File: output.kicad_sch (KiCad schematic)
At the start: 4 parts

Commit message: Cleaning up schematic
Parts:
- removed TP3: 5V Testpoint, MountingHole:MountingHole_6mm_Pad_TopBottom, symbol Connector:TestPoint
- removed TP4: 3.3v TestPoint, MountingHole:MountingHole_6mm_Pad_TopBottom, symbol Connector:TestPoint
- removed Testpoint1, Testpoint2: GND, MountingHole:MountingHole_6mm_Pad_TopBottom, symbol Connector:TestPoint
- added 3V3_HK1, 5V_HK1: TestPoint, _LVBus:HARWIN_S1751-46R, symbol Connector:TestPoint
- added C20, C21, C22: 10uf, Capacitor_SMD:C_1210_3225Metric, symbol Device:C
- added C23, C24, C27, C49, C50: 1uF, Capacitor_SMD:C_0603_1608Metric, symbol Device:C
- added C25: 10nF, Capacitor_SMD:C_0603_1608Metric, symbol Device:C
- added C26: 0.1uF, Capacitor_SMD:C_0603_1608Metric, symbol Device:C
- added C47: 4.7pF, Capacitor_SMD:C_0603_1608Metric, symbol Device:C
- added C48: 47uF, Capacitor_SMD:C_1210_3225Metric, symbol Device:C
- added D1: SMCJ26A, Diode_SMD:D_SMC, symbol Device:D_Zener
- added D2: SMF5.0A, Diode_SMD:D_SOD-123F, symbol Device:D_Zener
- added D3: SMF3.3, Diode_SMD:D_SOD-123F, symbol Device:D_Zener
- added FB5: FerriteBead, Inductor_SMD:L_1812_4532Metric, symbol Device:FerriteBead
- added L3: 1.5uH, _LVBus:Lair Inductor, symbol Device:L
- added R14: 18.22K, Resistor_SMD:R_0603_1608Metric, symbol Device:R_US
- added R15: 1M, Resistor_SMD:R_0603_1608Metric, symbol Device:R_US
- added R16: 243k, Resistor_SMD:R_0603_1608Metric, symbol Device:R_US
- added U4: LT8640SEV_PBF, _LVBus:CONV_LT8640SEV_PBF, symbol _LT8640S:LT8640SEV_PBF
- added U5: TLV75533PDBV, Package_TO_SOT_SMD:SOT-23-5, symbol Regulator_Linear:TLV75533PDBV
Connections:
- net GND: now also C20.2, C21.2, C22.2, C23.2, C24.2, C25.2, C27.2, C48.2, C49.2, C50.2, D1.2 (A), D2.2 (A), D3.2 (A), R14.2, R16.1, U4.16 (GND), U4.22 (GND), U4.25 (GND), U4.26 (GND), U4.27 (GND), U4.28 (GND), U4.3 (GND), U5.2 (GND)
- net LVBUS_3V3: now also 3V3_HK1.1, C50.1, D3.1 (K), U5.5 (OUT)
- net LVBUS_5V: now also 5V_HK1.1, C47.1, C48.1, D2.1 (K), L3.2, R15.1, U4.1 (BIAS)
- new net: C21.1, C22.1, C23.1, C24.1, FB5.2, U4.13 (VIN), U4.14 (VIN), U4.17 (EN), U4.5 (VIN), U4.6 (VIN)
- new net: C26.2, L3.1, U4.10 (SW), U4.11 (SW), U4.12 (SW), U4.8 (SW), U4.9 (SW)
- new net: R14.1, U4.18 (RT)
- new net: C27.1, U4.2 (INTVCC)
- new net: C25.1, U4.21 (TR/SS)
- new net: C47.2, R15.2, R16.2, U4.24 (FB)
- new net: C26.1, U4.7 (BST)
- new net HV_BUS: C20.1, D1.1 (K), FB5.1
- new net LV_BUS_5V: C49.1, U5.1 (IN), U5.3 (EN)
- no-connect marks 0 -> 9
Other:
- removed sheet LDO
- removed sheet buck_converter
- note added: "3V3 Regulator"
- note added: "5V Regulator"
- note added: "HV-LV Converter"
- note removed: "LVBus_3V3 Voltage"
- note removed: "LVBus_5V Voltage"

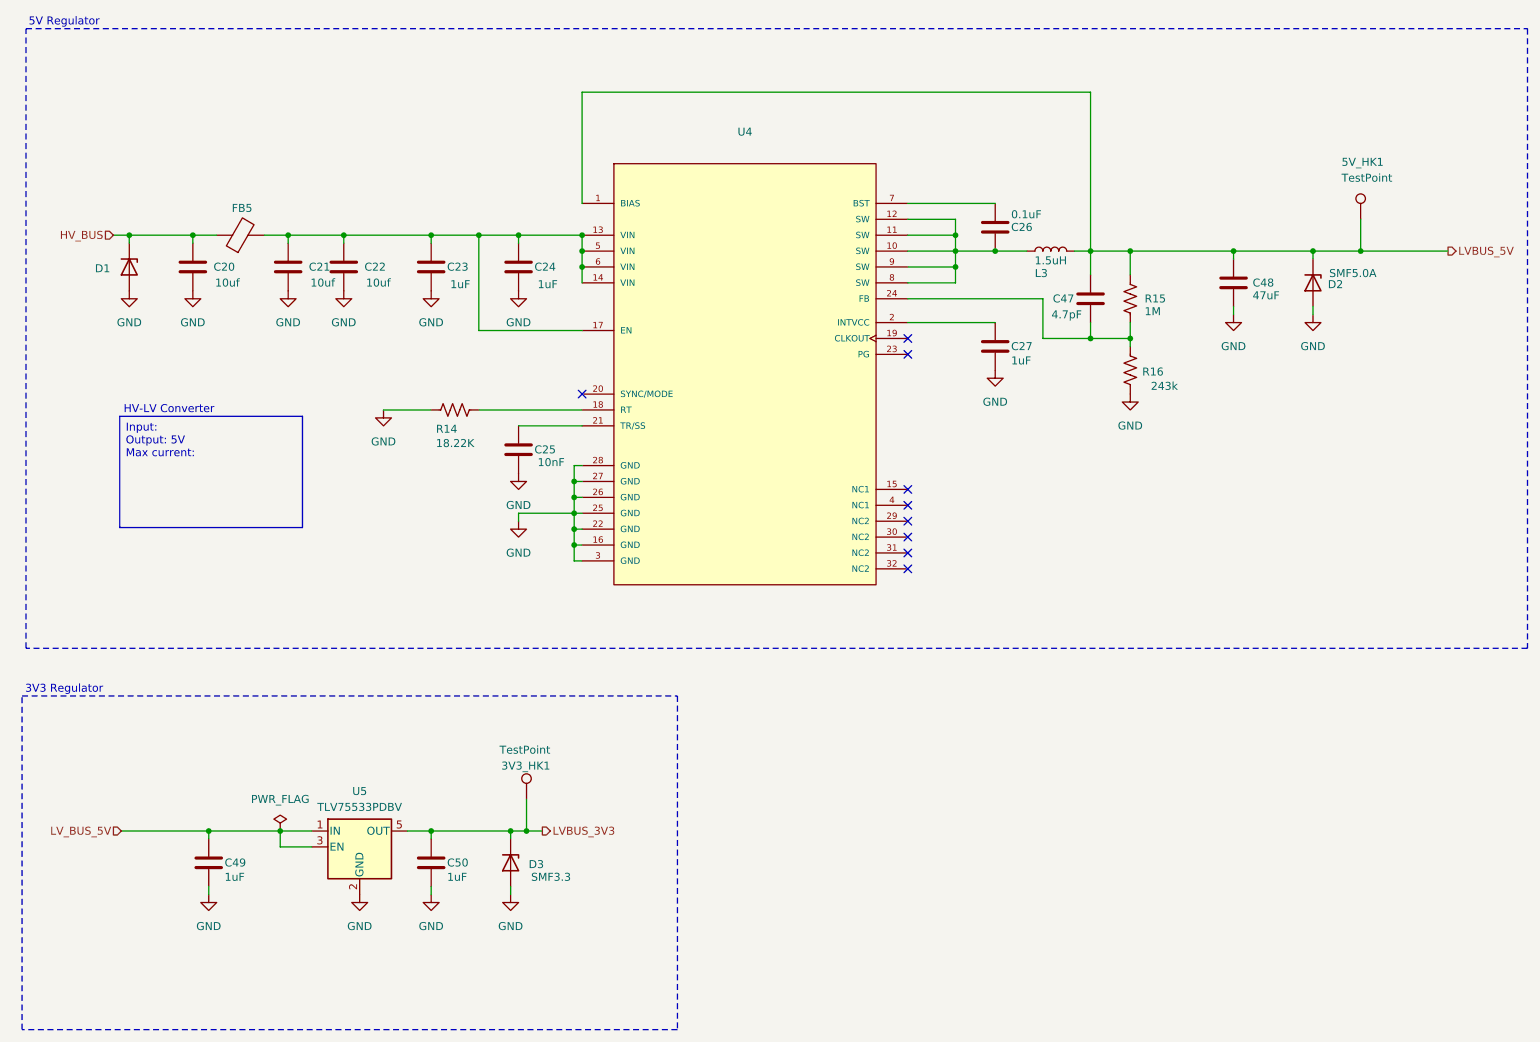
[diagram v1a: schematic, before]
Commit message: Starting bus load switch layout
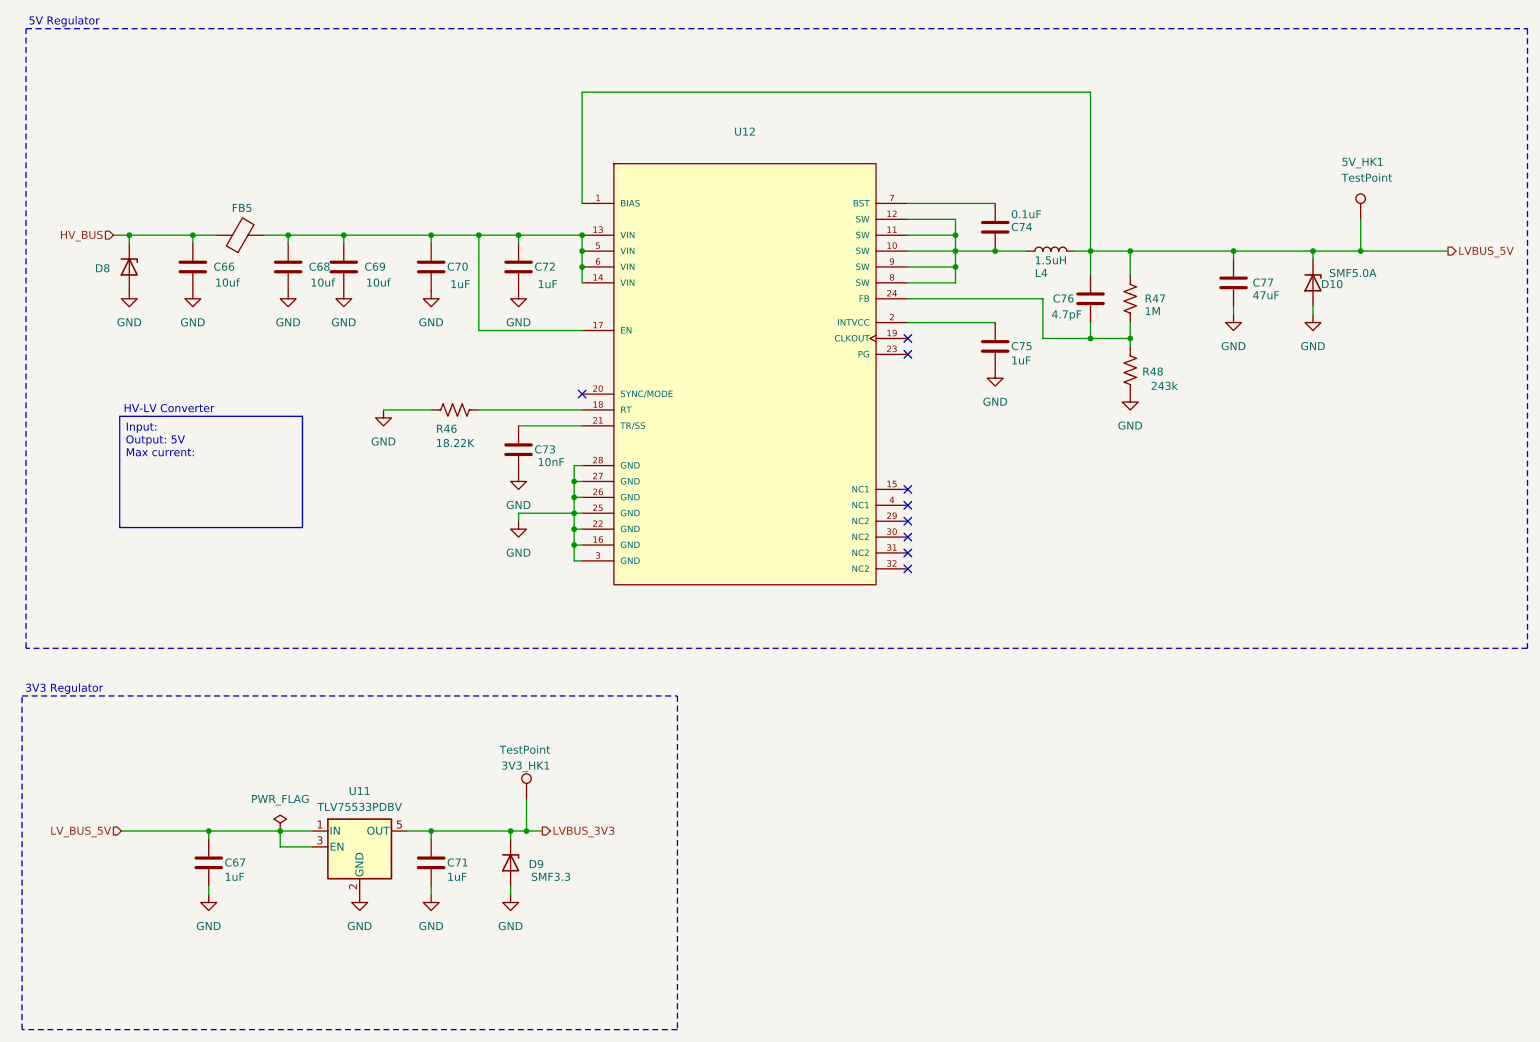
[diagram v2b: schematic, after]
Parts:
- renumbered C20 to C66, C49 to C67, C21 to C68, C22 to C69, C23 to C70, C50 to C71, C24 to C72, C25 to C73, C26 to C74, C27 to C75, C47 to C76, C48 to C77, D2 to D10, D1 to D8, D3 to D9, L3 to L4, R14 to R46, R15 to R47, R16 to R48, U5 to U11, U4 to U12

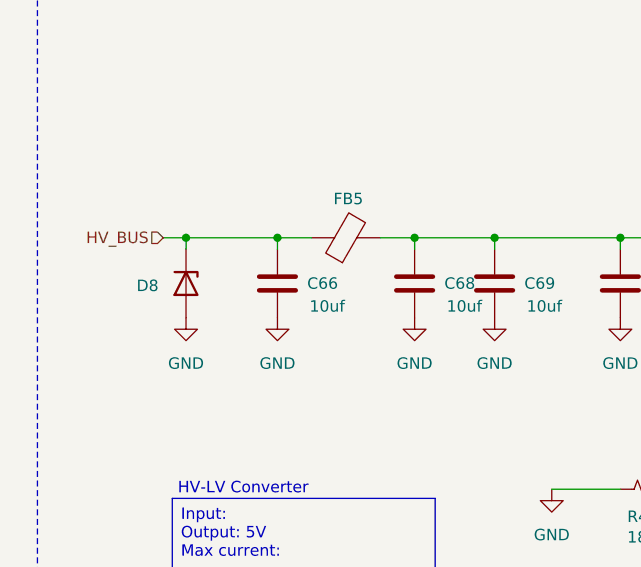
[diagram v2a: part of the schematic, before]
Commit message: Doing placement for 5V 3V3 IMU
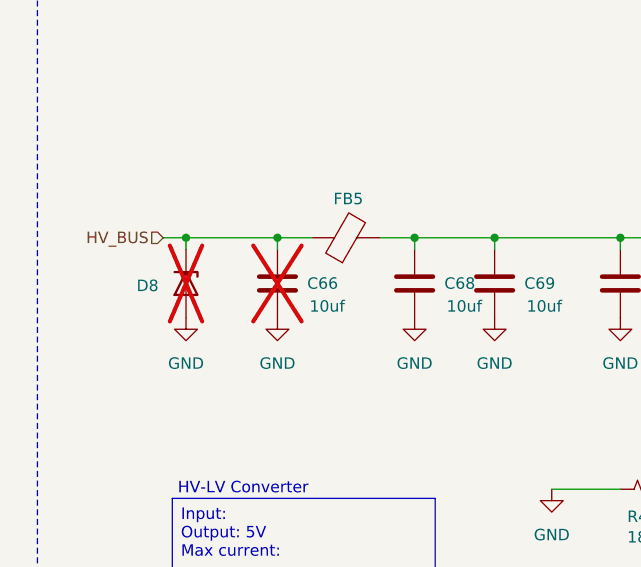
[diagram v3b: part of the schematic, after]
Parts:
- C66, D8: now not fitted; now left out of the parts list
- U12: footprint _LVBus:CONV_LT8640SEV_PBF -> _PowerBoard:CONV_LT8640SEV_PBF
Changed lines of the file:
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@@
 			)
 		)
-		(property "Footprint" "_LVBus:CONV_LT8640SEV_PBF"
+		(property "Footprint" "_PowerBoard:CONV_LT8640SEV_PBF"
 			(at 154.94 80.01 0)
 			(effects
@@
 		(unit 1)
 		(exclude_from_sim no)
-		(in_bom yes)
-		(on_board yes)
-		(dnp no)
+		(in_bom no)
+		(on_board no)
+		(dnp yes)
 		(property "Reference" "D8"
 			(at 52.832 61.214 90)
@@
 		(at 66.04 60.96 0)
 		(unit 1)
-		(exclude_from_sim no)
-		(in_bom yes)
-		(on_board yes)
-		(dnp no)
+		(exclude_from_sim yes)
+		(in_bom no)
+		(on_board no)
+		(dnp yes)
 		(property "Reference" "C66"
 			(at 69.342 60.96 0)

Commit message: Powerboard planning layout
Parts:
- removed 3V3_HK1, 5V_HK1: TestPoint, _LVBus:HARWIN_S1751-46R, symbol Connector:TestPoint
- L4: footprint _LVBus:Lair Inductor -> Inductor_SMD:Untitled

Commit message: Working on it
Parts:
- removed C74: 0.1uF, Capacitor_SMD:C_0603_1608Metric, symbol Device:C
- removed C75: 1uF, Capacitor_SMD:C_0603_1608Metric, symbol Device:C
- FB5: now not fitted; now left out of the parts list
- renumbered D8 to D10, D9 to D11, D10 to D12, R46 to R44, R47 to R45, R48 to R46
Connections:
- net LV_BUS_5V is gone; now on net +5V: C67.1, U11.1 (IN), U11.3 (EN)
- net HV_BUS: now also C68.1, C69.1, C70.1, C72.1, FB5.2, U12.13 (VIN), U12.14 (VIN), U12.17 (EN), U12.5 (VIN), U12.6 (VIN)
- net intvcc: now reaches U12.2 (INTVCC)
- net intvcc: now also U12.20 (SYNC/MODE)
- net LVBUS_3V3 renamed +3V3
- net LVBUS_5V renamed +5V
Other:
- moved on the sheet: C73, L4, R44

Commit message: Working on schematic and layout
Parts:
- renumbered C66 to C68, C67 to C69, C68 to C70, C69 to C71, C70 to C72, C71 to C73, C73 to C74, C72 to C75, R44 to R45, R45 to R46, R46 to R47, U11 to U12, U12 to U13

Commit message: Pushing
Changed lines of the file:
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@@
 		)
 	)
-	(text_box "Input:\nOutput: 5V\nMax current: "
+	(text_box "Input:\nOutput: 5V\nMax current: 6A"
 		(exclude_from_sim no)
 		(at 54.356 84.836 0)

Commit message: BOM in folder
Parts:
- C68, C70, C71: JLCPCB Status (none) -> Similar JLC in-stock package match; Mfr P/N CL32B106KBJNNWE -> CS3225X7R106K500NRL; Supplier_1 DigiKey -> LCSC; Supplier_1 P/N 1276-3388-2-ND -> C2918502; Supplier_1 Unit Price $0.22 -> (none)
- C69, C73: JLCPCB Status (none) -> JLC in-stock package match; Mfr P/N (none) -> CL10A105KB8NNNC; Supplier_1 DigiKey -> LCSC; Supplier_1 P/N 587-3247-2-ND -> C15849; Supplier_1 Unit Price $0.08 -> (none)
- C72, C75: JLCPCB Status (none) -> JLC in-stock package match; Mfr P/N UMK107AB7105KA-T -> CL10A105KB8NNNC; Supplier_1 DigiKey -> LCSC; Supplier_1 P/N 587-3247-2-ND -> C15849; Supplier_1 Unit Price $0.08 -> (none)
- C74: Supplier_1 DigiKey -> LCSC; Supplier_1 P/N 1276-1009-2-ND -> C57112; Supplier_1 Unit Price $0.08 -> (none)
- C76: JLCPCB Status (none) -> JLC in-stock package match; Mfr P/N GRM1885C1H4R7CA01D -> 0603CG4R7C500NT; Supplier_1 DigiKey -> LCSC; Supplier_1 P/N 490-12722-2-ND -> C1669; Supplier_1 Unit Price 0.12 -> (none)
- C77: Supplier_1 DigiKey -> LCSC; Supplier_1 P/N 1276-3376-2-ND -> C2932477; Supplier_1 Unit Price $0.68 -> (none)
- D10: Supplier_1 Digikey -> LCSC; Supplier_1 P/N SMCJ26ALFTR-ND -> C152085; Supplier_1 Unit Price 0.35000 -> (none)
- D11: Supplier_1 Digikey -> LCSC; Supplier_1 P/N F7701TR-ND -> C2649858; Supplier_1 Unit Price 0.49000 -> (none)
- D12: Supplier_1 DigiKey -> LCSC; Supplier_1 P/N 4878-SMF5.0ATR-ND -> C151296; Supplier_1 Unit Price 0.25000 -> (none)
- FB5: Supplier_1 DigiKey -> LCSC; Supplier_1 P/N 732-3431-2-ND -> C5155961; Supplier_1 Unit Price $0.68 -> (none)
- L4: Supplier_1 Digikey -> LCSC; Supplier_1 P/N 240-TYA40201R5M-10TR-ND -> C2649052; Supplier_1 Unit Price 0.37000 -> (none)
- R45: Supplier_1 Digikey -> LCSC; Supplier_1 P/N P18.2KDBTR-ND -> C22793; Supplier_1 Unit Price 0.10000 -> (none)
- R46: JLCPCB Status (none) -> JLC in-stock package match; Mfr P/N ERJ-3EKF1004V -> 0603WAF1004T5E; Supplier_1 DigiKey -> LCSC; Supplier_1 P/N P1.00MHTR-ND -> C22935; Supplier_1 Unit Price 0.10 -> (none)
- R47: JLCPCB Status (none) -> JLC in-stock package match; Mfr P/N ERA-3AEB2433V -> 0603WAF2433T5E; Supplier_1 DigiKey -> LCSC; Supplier_1 P/N P243KDBTR-ND -> C23351; Supplier_1 Unit Price 0.10 -> (none)
- U12: Supplier_1 Digikey -> LCSC; Supplier_1 P/N 296-50411-2-ND -> C404027; Supplier_1 Unit Price 0.36000 -> (none)
- U13: Supplier_1 Digikey -> LCSC; Supplier_1 P/N 505-LT8640SEV#PBF-ND -> C514429; Supplier_1 Unit Price 13.52000 -> (none)
